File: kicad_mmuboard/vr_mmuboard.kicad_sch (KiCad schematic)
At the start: 3 parts, among them J1 Conn_01x02_Male, U1 ST_MMU_SOCKET, U2 ST_MMU_PHY

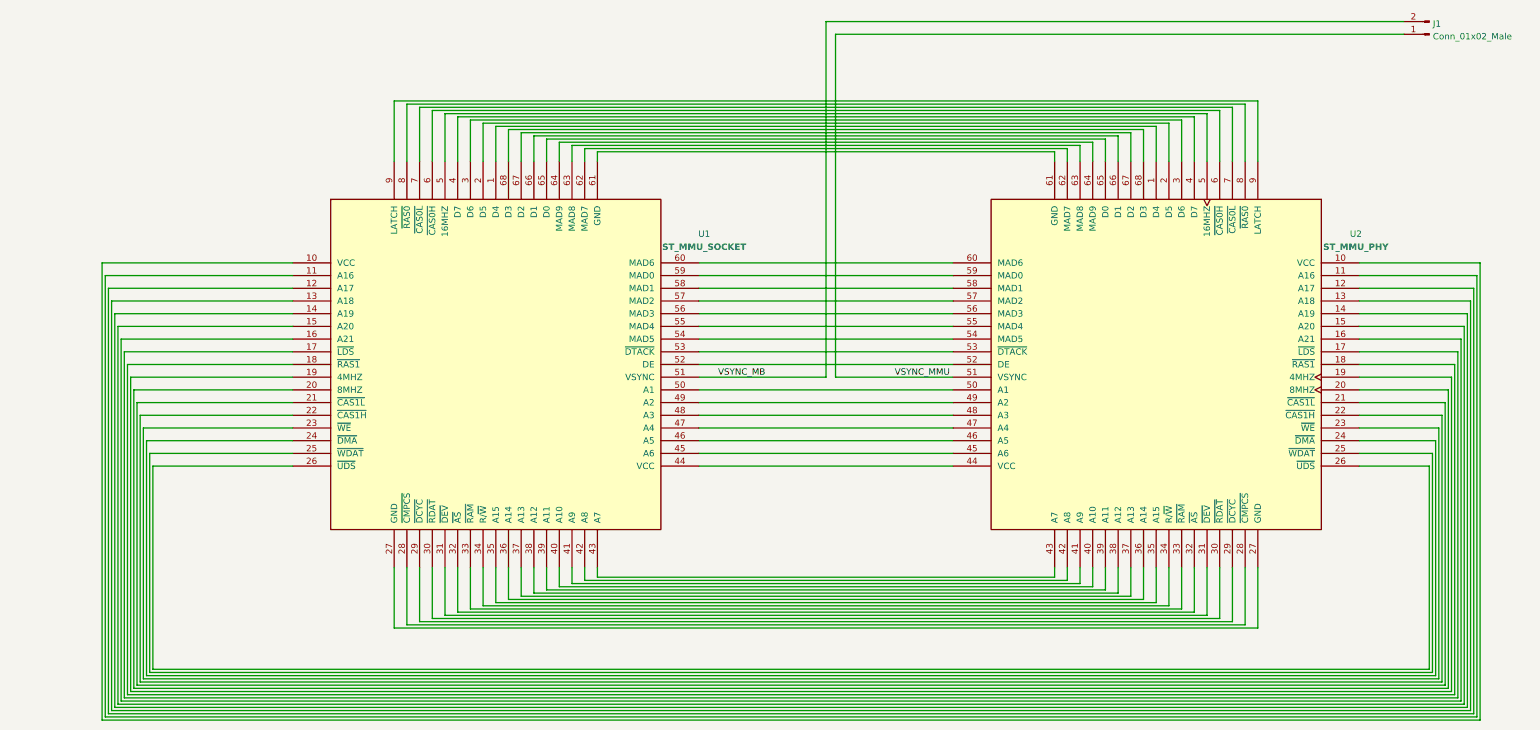
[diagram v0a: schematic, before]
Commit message: MMUBoard added to repo
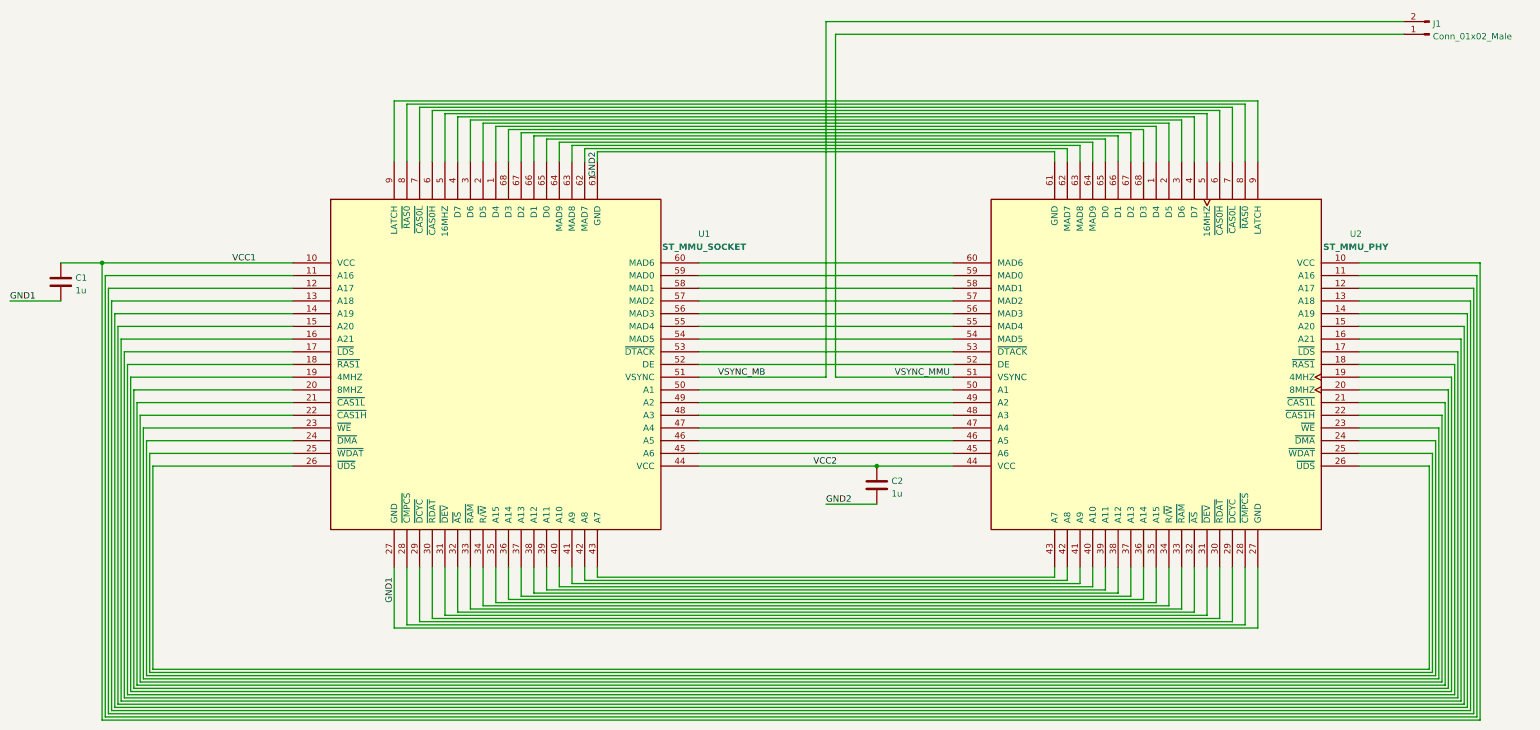
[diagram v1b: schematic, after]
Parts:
- added C1, C2: 1u, Capacitor_SMD:C_0805_2012Metric_Pad1.18x1.45mm_HandSolder, symbol Device:C
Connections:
- net VCC1: now reaches U1.10 (VCC), U2.10 (VCC)
- net VCC1: now also C1.1
- net GND1: now reaches U1.27 (GND), U2.27 (GND)
- net GND1: now also C1.2
- net VCC2: now reaches U1.44 (VCC), U2.44 (VCC)
- net VCC2: now also C2.1
- net GND2: now reaches U1.61 (GND), U2.61 (GND)
- net GND2: now also C2.2
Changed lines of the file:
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@@
     (comment 2 "Released under the terms of the GPLv2")
   )
+  (junction (at 52.07 109.22) (diameter 0) (color 0 0 0 0)
+  )
+  (junction (at 207.01 149.86) (diameter 0) (color 0 0 0 0)
+  )
   (wire (pts (xy 323.85 196.85) (xy 323.85 124.46))
     (stroke (width 0) (type default) (color 0 0 0 0))
@@
     (stroke (width 0) (type default) (color 0 0 0 0))
   )
-  (wire (pts (xy 222.25 149.86) (xy 171.45 149.86))
+  (wire (pts (xy 222.25 149.86) (xy 207.01 149.86))
     (stroke (width 0) (type default) (color 0 0 0 0))
   )
@@
     (stroke (width 0) (type default) (color 0 0 0 0))
   )
+  (wire (pts (xy 43.815 116.84) (xy 33.655 116.84))
+    (stroke (width 0) (type default) (color 0 0 0 0))
+  )
   (wire (pts (xy 128.27 81.28) (xy 265.43 81.28))
     (stroke (width 0) (type default) (color 0 0 0 0))
@@
     (stroke (width 0) (type default) (color 0 0 0 0))
   )
+  (wire (pts (xy 43.815 109.22) (xy 52.07 109.22))
+    (stroke (width 0) (type default) (color 0 0 0 0))
+  )
   (wire (pts (xy 143.51 170.18) (xy 143.51 173.99))
     (stroke (width 0) (type default) (color 0 0 0 0))
@@
     (stroke (width 0) (type default) (color 0 0 0 0))
   )
+  (wire (pts (xy 207.01 149.86) (xy 171.45 149.86))
+    (stroke (width 0) (type default) (color 0 0 0 0))
+  )
   (wire (pts (xy 222.25 121.92) (xy 171.45 121.92))
     (stroke (width 0) (type default) (color 0 0 0 0))
@@
     (stroke (width 0) (type default) (color 0 0 0 0))
   )
+  (wire (pts (xy 207.01 157.48) (xy 196.85 157.48))
+    (stroke (width 0) (type default) (color 0 0 0 0))
+  )
   (wire (pts (xy 59.69 193.04) (xy 59.69 139.7))
     (stroke (width 0) (type default) (color 0 0 0 0))
@@
   (wire (pts (xy 257.81 83.185) (xy 135.89 83.185))
     (stroke (width 0) (type default) (color 0 0 0 0))
+  )
+  (label "GND1" (at 33.655 116.84 0)
+    (effects (font (size 1.27 1.27)) (justify left bottom))
   )
   (label "VSYNC_MB" (at 175.26 132.08 0)
     (effects (font (size 1.27 1.27)) (justify left bottom))
   )
+  (label "VCC1" (at 78.105 109.22 0)
+    (effects (font (size 1.27 1.27)) (justify left bottom))
+  )
+  (label "GND2" (at 151.13 86.995 270)
+    (effects (font (size 1.27 1.27)) (justify right bottom))
+  )
+  (label "VCC2" (at 194.31 149.86 0)
+    (effects (font (size 1.27 1.27)) (justify left bottom))
+  )
   (label "VSYNC_MMU" (at 221.615 132.08 180)
     (effects (font (size 1.27 1.27)) (justify right bottom))
+  )
+  (label "GND1" (at 110.49 172.085 270)
+    (effects (font (size 1.27 1.27)) (justify right bottom))
+  )
+  (label "GND2" (at 196.85 157.48 0)
+    (effects (font (size 1.27 1.27)) (justify left bottom))
   )
   (symbol (lib_id "st_mmu:ST_MMU_SOCKET") (at 130.81 129.54 0) (unit 1)
@@
     (pin "2")
   )
+  (symbol (lib_id "Device:C") (at 43.815 113.03 0) (unit 1)
+    (in_bom yes) (on_board yes) (fields_autoplaced)
+    (property "Reference" "C1" (id 0) (at 46.736 112.1953 0)
+      (effects (font (size 1.27 1.27)) (justify left))
+    )
+    (property "Value" "1u" (id 1) (at 46.736 114.7322 0)
+      (effects (font (size 1.27 1.27)) (justify left))
+    )
+    (property "Footprint" "Capacitor_SMD:C_0805_2012Metric_Pad1.18x1.45mm_HandSolder" (id 2) (at 44.7802 116.84 0)
+      (effects (font (size 1.27 1.27)) hide)
+    )
+    (property "Datasheet" "~" (id 3) (at 43.815 113.03 0)
+      (effects (font (size 1.27 1.27)) hide)
+    )
+    (pin "1")
+    (pin "2")
+  )
+  (symbol (lib_id "Device:C") (at 207.01 153.67 0) (unit 1)
+    (in_bom yes) (on_board yes) (fields_autoplaced)
+    (property "Reference" "C2" (id 0) (at 209.931 152.8353 0)
+      (effects (font (size 1.27 1.27)) (justify left))
+    )
+    (property "Value" "1u" (id 1) (at 209.931 155.3722 0)
+      (effects (font (size 1.27 1.27)) (justify left))
+    )
+    (property "Footprint" "Capacitor_SMD:C_0805_2012Metric_Pad1.18x1.45mm_HandSolder" (id 2) (at 207.9752 157.48 0)
+      (effects (font (size 1.27 1.27)) hide)
+    )
+    (property "Datasheet" "~" (id 3) (at 207.01 153.67 0)
+      (effects (font (size 1.27 1.27)) hide)
+    )
+    (pin "1")
+    (pin "2")
+  )
   (symbol (lib_id "st_mmu:ST_MMU_PHY") (at 262.89 129.54 0) (mirror y) (unit 1)
     (in_bom yes) (on_board yes) (fields_autoplaced)
@@
   )
   (symbol_instances
+    (path "/79ef956d-fc6b-4724-9497-a4a97bf6e964"
+      (reference "C1") (unit 1) (value "1u") (footprint "Capacitor_SMD:C_0805_2012Metric_Pad1.18x1.45mm_HandSolder")
+    )
+    (path "/9a847c94-9554-4caa-9c10-68c2c28960f2"
+      (reference "C2") (unit 1) (value "1u") (footprint "Capacitor_SMD:C_0805_2012Metric_Pad1.18x1.45mm_HandSolder")
+    )
     (path "/6b7c5710-a72a-49d1-8efa-b6d8f94c79b6"
       (reference "J1") (unit 1) (value "Conn_01x02_Male") (footprint "Connector_PinHeader_2.54mm:PinHeader_1x02_P2.54mm_Horizontal")
